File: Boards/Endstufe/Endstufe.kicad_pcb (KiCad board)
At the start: 2 copper layers, 153 x 111 mm, 64 parts, among them J1 HV In, J2 Relais, J3 NF_In, J4 Trafo, K1 G6E, P4 6V3_AC, P5 Trafo_GK, P6 6V3_DC, P7 VSup1, P8 Bias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

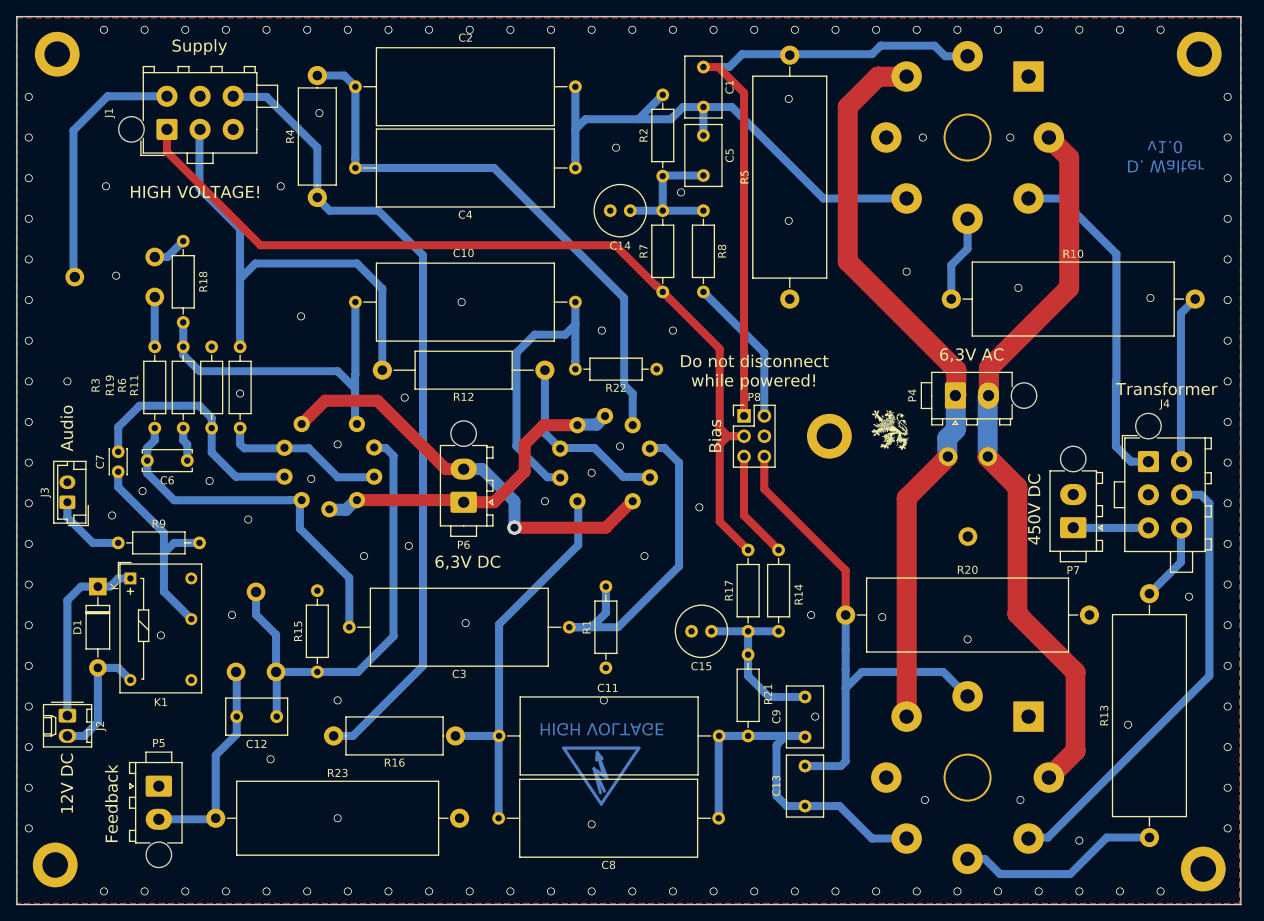
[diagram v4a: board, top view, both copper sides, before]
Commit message: Added Test, moved mounting holes
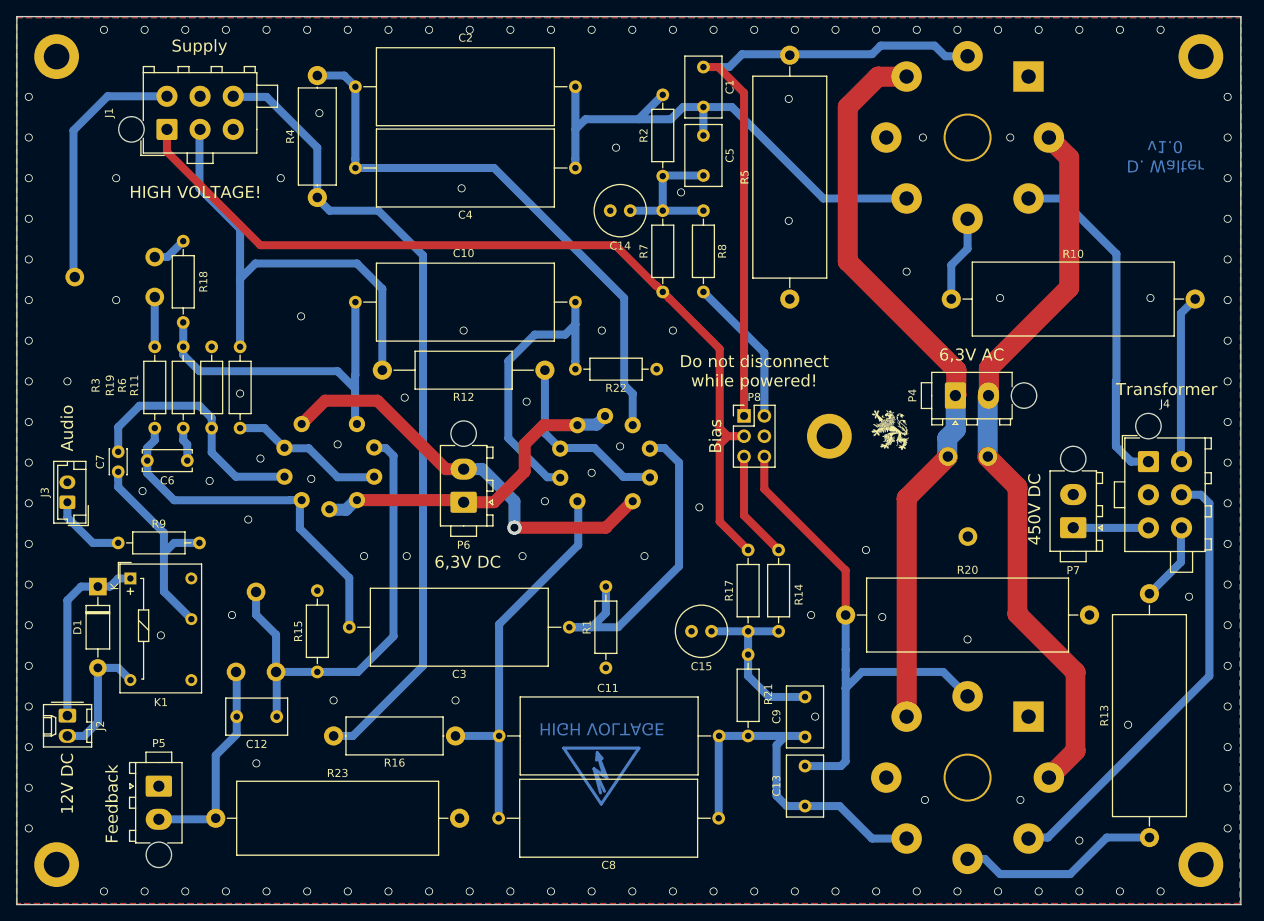
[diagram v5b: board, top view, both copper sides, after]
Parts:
- moved REF** 0.63 mm to (207.0, 157.2)
- moved REF** 0.37 mm to (207.0, 56.2)
- moved REF** 0.31 mm to (63.9, 56.2)
- moved REF** 0.18 mm to (63.9, 157.2)
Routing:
- net Net-(R11-Pad1): track 20.3 -> 19.1 mm
- net Net-(C10-Pad1): track 36.1 -> 36.9 mm
- net GND: vias 142 -> 143
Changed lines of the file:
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@@
     (thickness 1.6)
     (drawings 22)
-    (tracks 447)
+    (tracks 448)
     (zones 0)
     (modules 64)
@@
   )
   (module MountingHole:MountingHole_3.2mm_M3_DIN965_Pad (layer F.Cu)
-    (at 64.008 55.88)
+    (at 63.928 56.181)
     (descr "Mounting Hole 3.2mm, M3, DIN965")
     (tags "mounting hole 3.2mm m3 din965")
@@
   )
   (module MountingHole:MountingHole_3.2mm_M3_DIN965_Pad (layer F.Cu)
-    (at 63.754 157.226)
+    (at 63.928 157.179)
     (descr "Mounting Hole 3.2mm, M3, DIN965")
     (tags "mounting hole 3.2mm m3 din965")
@@
   )
   (module MountingHole:MountingHole_3.2mm_M3_DIN965_Pad (layer F.Cu)
-    (at 207.264 157.734)
+    (at 206.963 157.179)
     (descr "Mounting Hole 3.2mm, M3, DIN965")
     (tags "mounting hole 3.2mm m3 din965")
@@
   )
   (module MountingHole:MountingHole_3.2mm_M3_DIN965_Pad (layer F.Cu)
-    (at 206.756 55.88)
+    (at 206.963 56.181)
     (descr "Mounting Hole 3.2mm, M3, DIN965")
     (tags "mounting hole 3.2mm m3 din965")
@@
   (gr_circle (center 177.8 66.04) (end 202.8 74.676) (layer Dwgs.User) (width 0.2))
   (gr_circle (center 177.8 146.304) (end 177.8 171.304) (layer Dwgs.User) (width 0.2))
-  (via (at 210.312 61.214) (size 1) (drill 0.8) (layers F.Cu B.Cu) (net 7))
-  (via (at 95.758 108.966) (size 1) (drill 0.8) (layers F.Cu B.Cu) (net 7))
-  (via (at 134.366 104.902) (size 1) (drill 0.8) (layers F.Cu B.Cu) (net 7))
   (segment (start 180.310747 106.241253) (end 180.310747 98.703173) (width 2.5) (layer B.Cu) (net 1) (status 30))
   (segment (start 180.3 106.252) (end 180.310747 106.241253) (width 2.5) (layer F.Cu) (net 1))
@@
   (segment (start 121.158 115.062) (end 121.158 111.76) (width 1.5) (layer B.Cu) (net 4))
   (segment (start 121.158 111.76) (end 117.145 107.747) (width 1.5) (layer B.Cu) (net 4))
-  (segment (start 86.868 104.62768) (end 86.868 102.616) (width 1) (layer B.Cu) (net 5) (status 20))
-  (segment (start 87.38616 105.14584) (end 86.868 104.62768) (width 1) (layer B.Cu) (net 5))
-  (segment (start 95.447675 105.14584) (end 87.38616 105.14584) (width 1) (layer B.Cu) (net 5))
-  (segment (start 103.39832 108.7628) (end 99.064635 108.7628) (width 1) (layer B.Cu) (net 5) (status 10))
+  (segment (start 89.916 102.616) (end 86.868 102.616) (width 1) (layer B.Cu) (net 5))
+  (segment (start 92.44584 105.14584) (end 89.916 102.616) (width 1) (layer B.Cu) (net 5))
+  (segment (start 95.447675 105.14584) (end 92.44584 105.14584) (width 1) (layer B.Cu) (net 5))
+  (segment (start 103.39832 108.7628) (end 99.064635 108.7628) (width 1) (layer B.Cu) (net 5))
   (segment (start 99.064635 108.7628) (end 95.447675 105.14584) (width 1) (layer B.Cu) (net 5))
   (segment (start 92.18168 108.7628) (end 92.086697 108.667817) (width 1) (layer B.Cu) (net 6) (status 30))
@@
   (segment (start 71.628 105.577) (end 71.628 102.489) (width 1) (layer B.Cu) (net 6))
   (segment (start 71.628 102.489) (end 74.295 99.822) (width 1) (layer B.Cu) (net 6))
+  (via (at 210.312 61.214) (size 1) (drill 0.8) (layers F.Cu B.Cu) (net 7))
+  (via (at 95.758 108.966) (size 1) (drill 0.8) (layers F.Cu B.Cu) (net 7))
+  (via (at 134.366 104.902) (size 1) (drill 0.8) (layers F.Cu B.Cu) (net 7))
   (segment (start 86.106 65.38) (end 86.004 65.278) (width 1) (layer B.Cu) (net 7))
   (via (at 69.85 160.528) (size 1) (drill 0.8) (layers F.Cu B.Cu) (net 7))
-  (via (at 99.06 151.384) (size 1) (drill 0.8) (layers F.Cu B.Cu) (net 7))
-  (via (at 107.95 117.348) (size 1) (drill 0.8) (layers F.Cu B.Cu) (net 7))
+  (via (at 113.792 136.652) (size 1) (drill 0.8) (layers F.Cu B.Cu) (net 7))
+  (via (at 107.696 118.618) (size 1) (drill 0.8) (layers F.Cu B.Cu) (net 7))
   (via (at 85.852 125.984) (size 1) (drill 0.8) (layers F.Cu B.Cu) (net 7))
   (via (at 76.962 128.524) (size 1) (drill 0.8) (layers F.Cu B.Cu) (net 7))
@@
   (via (at 130.81 108.204) (size 1) (drill 0.8) (layers F.Cu B.Cu) (net 7))
   (via (at 74.676 110.49) (size 1) (drill 0.8) (layers F.Cu B.Cu) (net 7))
-  (via (at 70.866 113.538) (size 1) (drill 0.8) (layers F.Cu B.Cu) (net 7))
-  (via (at 130.81 152.146) (size 1) (drill 0.8) (layers F.Cu B.Cu) (net 7))
-  (via (at 132.334 136.652) (size 1) (drill 0.8) (layers F.Cu B.Cu) (net 7))
-  (via (at 115.062 127) (size 1) (drill 0.8) (layers F.Cu B.Cu) (net 7))
+  (via (at 122.174 118.618) (size 1) (drill 0.8) (layers F.Cu B.Cu) (net 7))
   (via (at 137.414 118.618) (size 1) (drill 0.8) (layers F.Cu B.Cu) (net 7))
   (via (at 102.362 118.618) (size 1) (drill 0.8) (layers F.Cu B.Cu) (net 7))
@@
   (via (at 94.488 88.646) (size 1) (drill 0.8) (layers F.Cu B.Cu) (net 7))
   (via (at 132.08 90.424) (size 1) (drill 0.8) (layers F.Cu B.Cu) (net 7))
-  (via (at 114.554 86.868) (size 1) (drill 0.8) (layers F.Cu B.Cu) (net 7))
+  (via (at 114.808 90.424) (size 1) (drill 0.8) (layers F.Cu B.Cu) (net 7))
   (via (at 96.774 63.246) (size 1) (drill 0.8) (layers F.Cu B.Cu) (net 7))
-  (via (at 91.948 72.39) (size 1) (drill 0.8) (layers F.Cu B.Cu) (net 7))
-  (via (at 70.104 72.39) (size 1) (drill 0.8) (layers F.Cu B.Cu) (net 7))
-  (via (at 71.374 83.566) (size 1) (drill 0.8) (layers F.Cu B.Cu) (net 7))
+  (via (at 91.948 71.374) (size 1) (drill 0.8) (layers F.Cu B.Cu) (net 7))
+  (via (at 71.374 71.374) (size 1) (drill 0.8) (layers F.Cu B.Cu) (net 7))
+  (via (at 71.374 86.614) (size 1) (drill 0.8) (layers F.Cu B.Cu) (net 7))
   (via (at 140.97 90.424) (size 1) (drill 0.8) (layers F.Cu B.Cu) (net 7))
   (via (at 133.858 67.564) (size 1) (drill 0.8) (layers F.Cu B.Cu) (net 7))
@@
   (via (at 172.212 66.294) (size 1) (drill 0.8) (layers F.Cu B.Cu) (net 7))
   (via (at 183.134 66.294) (size 1) (drill 0.8) (layers F.Cu B.Cu) (net 7))
-  (via (at 184.15 85.09) (size 1) (drill 0.8) (layers F.Cu B.Cu) (net 7))
+  (via (at 181.864 86.36) (size 1) (drill 0.8) (layers F.Cu B.Cu) (net 7))
   (via (at 170.18 83.058) (size 1) (drill 0.8) (layers F.Cu B.Cu) (net 7))
   (via (at 200.66 86.36) (size 1) (drill 0.8) (layers F.Cu B.Cu) (net 7))
@@
   (via (at 197.866 139.7) (size 1) (drill 0.8) (layers F.Cu B.Cu) (net 7))
   (via (at 205.486 123.698) (size 1) (drill 0.8) (layers F.Cu B.Cu) (net 7))
-  (via (at 99.06 136.652) (size 1) (drill 0.8) (layers F.Cu B.Cu) (net 7))
+  (via (at 98.552 136.652) (size 1) (drill 0.8) (layers F.Cu B.Cu) (net 7))
   (via (at 141.986 73.152) (size 1) (drill 0.8) (layers F.Cu B.Cu) (net 7))
   (via (at 74.93 160.528) (size 1) (drill 0.8) (layers F.Cu B.Cu) (net 7))
@@
   (via (at 86.868 98.298) (size 1) (drill 0.8) (layers F.Cu B.Cu) (net 7))
   (via (at 65.278 96.774) (size 1) (drill 0.8) (layers F.Cu B.Cu) (net 7))
-  (via (at 90.678 144.018) (size 1) (drill 0.8) (layers F.Cu B.Cu) (net 7))
+  (via (at 88.9 144.526) (size 1) (drill 0.8) (layers F.Cu B.Cu) (net 7))
   (via (at 158.75 138.684) (size 1) (drill 0.8) (layers F.Cu B.Cu) (net 7))
   (via (at 158.242 125.984) (size 1) (drill 0.8) (layers F.Cu B.Cu) (net 7))
@@
   (via (at 210.312 147.574) (size 1) (drill 0.8) (layers F.Cu B.Cu) (net 7))
   (via (at 210.312 152.654) (size 1) (drill 0.8) (layers F.Cu B.Cu) (net 7))
+  (via (at 114.554 72.644) (size 1) (drill 0.8) (layers F.Cu B.Cu) (net 7))
+  (via (at 165.1 117.856) (size 1) (drill 0.8) (layers F.Cu B.Cu) (net 7))
+  (via (at 89.408 106.426) (size 1) (drill 0.8) (layers F.Cu B.Cu) (net 7))
+  (via (at 122.682 99.314) (size 1) (drill 0.8) (layers F.Cu B.Cu) (net 7))
   (segment (start 128.016 127.508) (end 129.54 127.508) (width 1) (layer B.Cu) (net 8))
   (segment (start 132.588 125.73) (end 130.81 127.508) (width 1) (layer B.Cu) (net 8))
@@
   (segment (start 127.508 90.932) (end 128.778 89.662) (width 1) (layer B.Cu) (net 18))
   (segment (start 123.698 90.932) (end 127.508 90.932) (width 1) (layer B.Cu) (net 18))
-  (segment (start 121.412 93.218) (end 123.698 90.932) (width 1) (layer B.Cu) (net 18))
-  (segment (start 121.412 104.902) (end 121.412 93.218) (width 1) (layer B.Cu) (net 18))
+  (segment (start 120.396 94.234) (end 123.698 90.932) (width 1) (layer B.Cu) (net 18))
+  (segment (start 120.396 103.886) (end 120.396 94.234) (width 1) (layer B.Cu) (net 18))
   (segment (start 126.97968 108.7628) (end 125.2728 108.7628) (width 1) (layer B.Cu) (net 18))
-  (segment (start 125.2728 108.7628) (end 121.412 104.902) (width 1) (layer B.Cu) (net 18))
+  (segment (start 125.2728 108.7628) (end 120.396 103.886) (width 1) (layer B.Cu) (net 18))
   (segment (start 66.2 83.733) (end 66.04 83.573) (width 1) (layer B.Cu) (net 19))
   (segment (start 66.04 83.573) (end 66.04 65.405) (width 1) (layer B.Cu) (net 19))

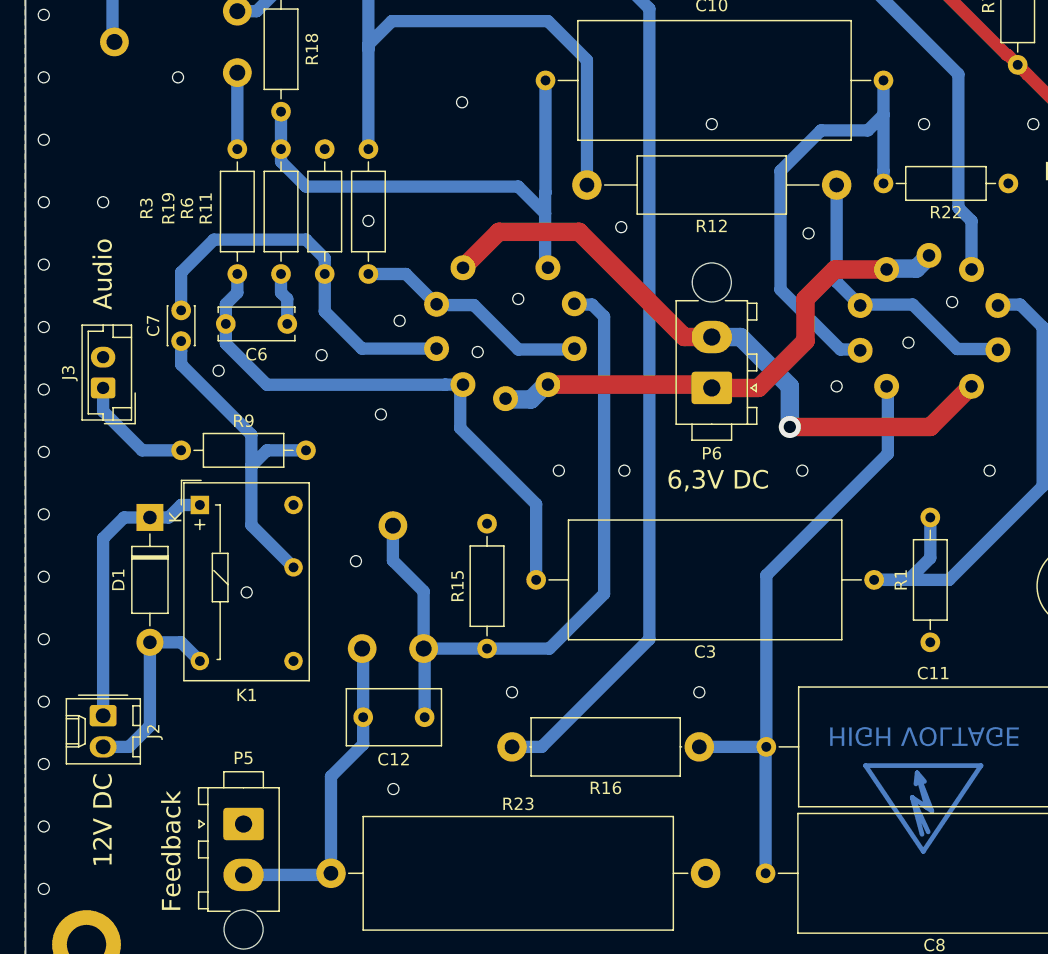
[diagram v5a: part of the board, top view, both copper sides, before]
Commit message: Adjusted Silkscreen
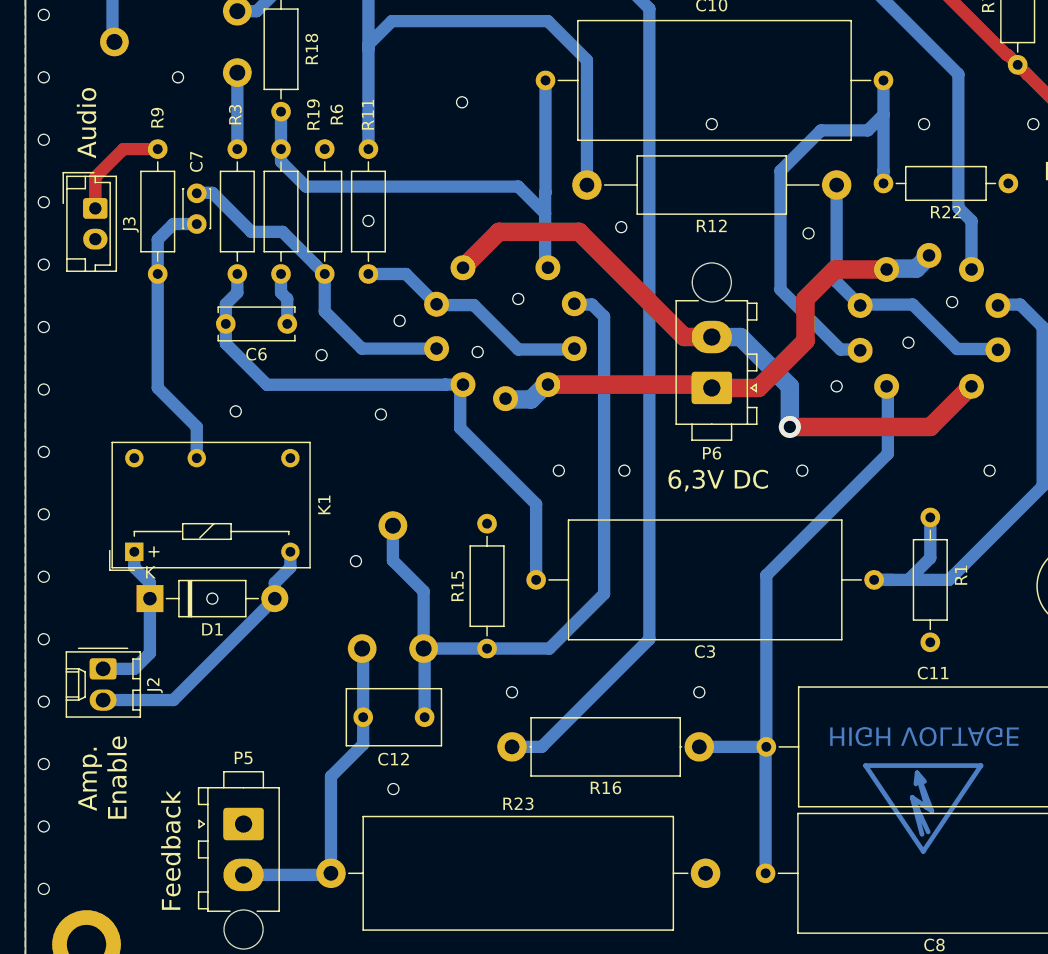
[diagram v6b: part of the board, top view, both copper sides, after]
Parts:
- moved R9 24.6 mm to (69.7, 92.5), turned to 270 degrees
- moved J3 14.6 mm to (64.6, 97.3), turned to 270 degrees
- moved C7 9.61 mm to (72.9, 98.6)
- moved D1 6.60 mm to (69.1, 129.0), turned to 0 degrees
- moved K1 6.55 mm to (67.8, 125.2), turned to 90 degrees
- moved J2 3.81 mm to (65.3, 134.7)
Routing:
- net Net-(D1-Pad1): track 23.4 -> 13.1 mm
- net Net-(D1-Pad2): track 16.0 -> 21.7 mm
- net Net-(C7-Pad2): track 31.3 -> 26.7 mm
- net Net-(C7-Pad1): track 27.2 -> 22.8 mm
- net Net-(J3-Pad1): track 9.57 -> 8.57 mm
- net GND: vias 143 -> 142
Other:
- board text added: "Amp. Enable"
- board text removed: "12V DC"
